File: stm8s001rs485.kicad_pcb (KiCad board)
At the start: 2 copper layers, 33.3 x 6.3 mm, 20 parts, among them J1 Conn_02x02_Odd_Even, J2 Conn_02x03_Counter_Clockwise, U1 DS1621S, U2 STM8S001J3M, U3 XC6206P332MR, U4 SP3485CN

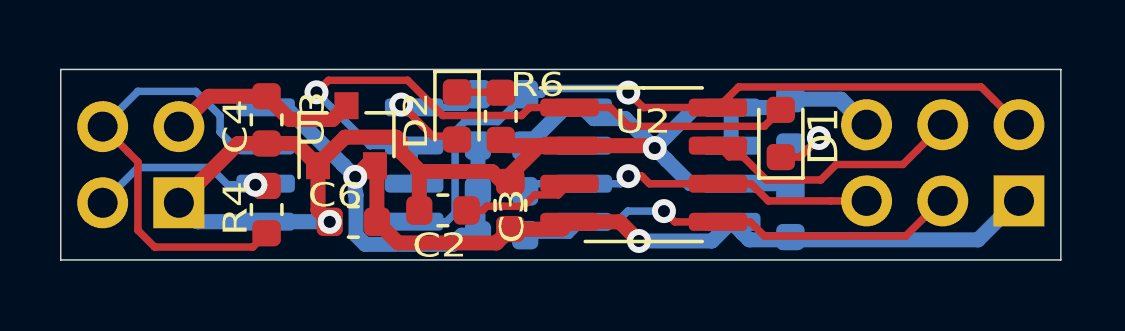
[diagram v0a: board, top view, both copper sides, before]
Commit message: Improved component placement
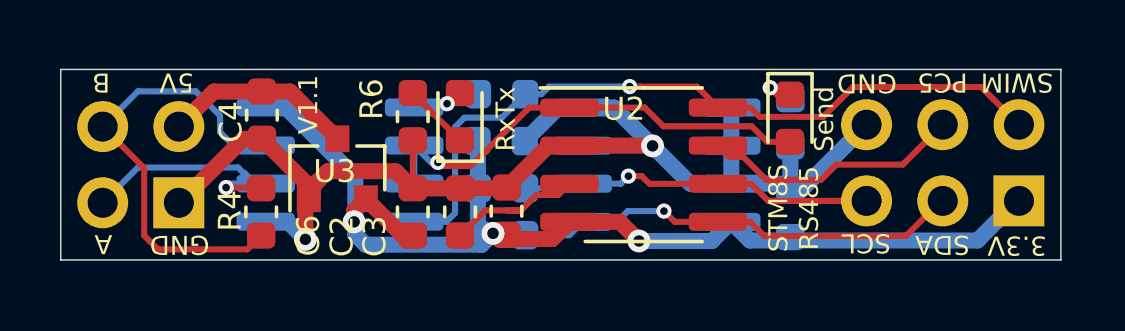
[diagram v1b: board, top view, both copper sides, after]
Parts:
- removed D1: LED red, LED_SMD:LED_0603_1608Metric
- added Send: LED red, LED_SMD:LED_0603_1608Metric, F.Cu at (169.5, 84.8)
- moved R6 2.93 mm to (156.9, 84.8)
- moved C6 2.01 mm to (156.9, 87.9), turned to 270 degrees
- moved U3 1.15 mm to (154.4, 86.5)
- moved C2 0.57 mm to (158.5, 87.9), turned to 270 degrees
- moved C3 0.23 mm to (160.0, 87.9)
- moved C4 0.22 mm to (151.9, 84.7)
- moved R4 0.20 mm to (151.8, 87.9)
- moved C1 0.15 mm to (159.8, 85.6)
- moved RxTx 0.10 mm to (158.5, 84.8), turned to 90 degrees
- moved R2 0.10 mm to (159.9, 87.1)
- turned R5 to 270 degrees
- renumbered D2 to RxTx
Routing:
- net GND: track 53.7 -> 43.3 mm
- net /DIR.RX: track 21.7 -> 15.4 mm
- net /A: track 6.21 -> 8.80 mm
- net +3V3: track 39.1 -> 36.9 mm, vias 2 -> 3
- net Net-(D2-Pad2): track 4.62 -> 3.06 mm
- net Net-(C2-Pad2): track 3.80 -> 4.80 mm
- net Net-(D1-Pad1): track 2.45 -> 1.59 mm
- net Net-(D2-Pad1): track 1.52 -> 2.23 mm
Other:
- net class Default: clearance 0.2 -> 0.2032; trace_width 0.25 -> 0.2032; via_dia 0.8 -> 0.508; via_drill 0.4 -> 0.254
- net class Power: clearance 0.2 -> 0.2032; trace_width 0.5 -> 0.5334; via_dia 0.8 -> 0.762; via_drill 0.4 -> 0.381
- rule trace_clearance: 0.2 -> 0.2032
- rule trace_min: 0.2 -> 0.1524
- rule via_min_drill: 0.3 -> 0.254
- rule via_min_size: 0.4 -> 0.508
- board text added: "3.3V"
- board text added: "5V"
- board text added: "A"
- board text added: "B"
- board text added: "GND"
- board text added: "PC5"
- board text added: "SCL"
- board text added: "SDA"
- board text added: "STM8S RS485"
- board text added: "SWIM"
- board text added: "V1.1"
